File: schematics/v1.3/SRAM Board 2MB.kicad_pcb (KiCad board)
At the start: 2 copper layers, 125.7 x 33 mm, 48 parts, among them J1 Conn_01x01, J10 Conn_01x01, J11 Conn_01x01, J12 Conn_01x01, J13 Conn_01x01, J14 Conn_01x01, J15 Conn_01x01, J16 Conn_01x01, J17 Conn_01x01, J18 Conn_01x01, J19 Conn_01x01, J2 Conn_01x01, J20 Conn_01x01, J21 Conn_01x01, J22 Conn_01x01, J23 Conn_01x01, J24 Conn_01x01, J25 Conn_01x01, J26 Conn_01x01, J27 Conn_01x01, J28 Conn_01x01, J29 Conn_01x01, J3 Conn_01x01, J30 Conn_01x01, J31 Conn_01x01, J32 Conn_01x01, J4 Conn_01x01, J5 Conn_01x01, J6 Conn_01x01, J7 Conn_01x01, J8 Conn_01x01, J9 Conn_01x01, U1 74ABT00, U2 74ABT821ADW, U3 74ABT32, U34 74LS373, U4 CY62157ESL-45ZSXI, U5 CY62157ESL-45ZSXI, U6 74ABT373, U7 74AHCT1G79

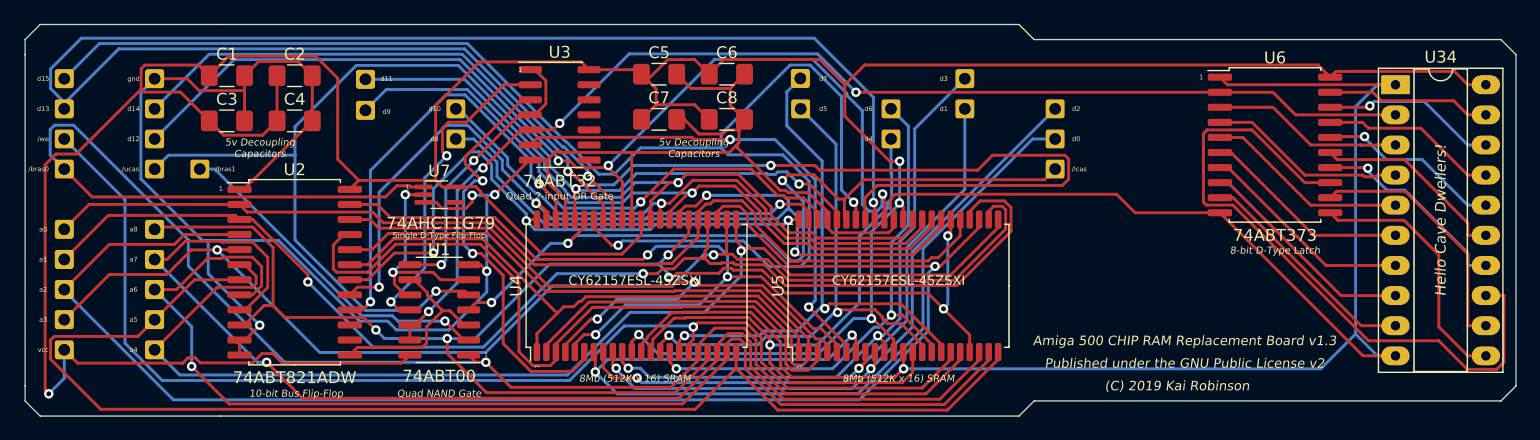
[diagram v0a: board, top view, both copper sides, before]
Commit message: Changed back to 2 layer board
Changed to 2 layer board, using thicker power traces and a copper fill on both sides for VCC and GND planes.
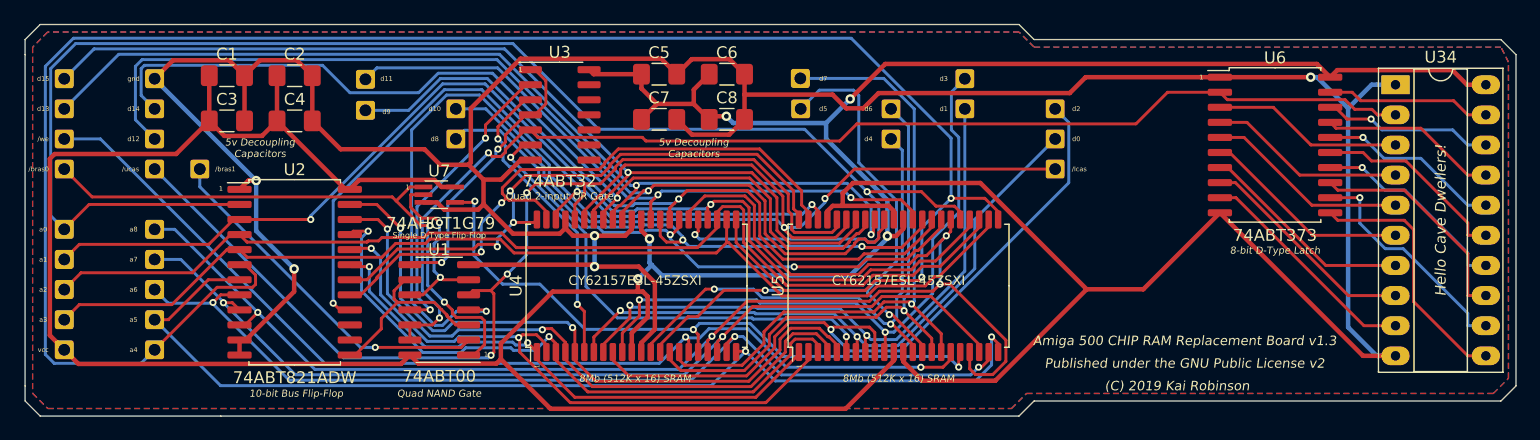
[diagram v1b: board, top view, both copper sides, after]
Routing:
- net /_bras0: track 132.7 -> 50.7 mm, vias 1 -> 2
- net /a4: track 96.9 -> 166.0 mm, vias 1 -> 2
- net /d13: track 142.0 -> 82.9 mm
- net /a18: track 0.00 -> 54.9 mm, vias 0 -> 3
- net /a0: track 86.9 -> 135.4 mm, vias 0 -> 2
- net /_lcas: track 68.5 -> 116.4 mm
- net /d15: track 123.7 -> 82.6 mm, vias 2 -> 1
- net /a2: track 129.1 -> 89.4 mm, vias 1 -> 0
- net /5d: track 57.0 -> 19.1 mm
- net /d14: track 112.5 -> 79.8 mm, vias 2 -> 1
- net /d0: track 78.7 -> 53.3 mm
- net /ma3: track 72.6 -> 52.5 mm, vias 0 -> 2
- net /a5: track 108.0 -> 88.9 mm, vias 0 -> 2
- net /a7: track 99.4 -> 81.7 mm, vias 1 -> 2
- net /a6: track 99.4 -> 81.8 mm, vias 1 -> 3
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- added copper zone on B.Cu, net GND
- added copper zone on F.Cu, net VCC
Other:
- net class Default: via_dia 0.8 -> 0.6; via_drill 0.4 -> 0.3
- net class Power added: clearance 0.2, trace_width 0.381, via_dia 0.8, via_drill 0.4
- rule trace_min: 0.2 -> 0.1
- rule via_min_drill: 0.3 -> 0.2

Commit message: New Board Layout
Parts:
- moved J18 64.5 mm to (218.9, 82.0)
- moved C8 47.8 mm to (245.4, 88.9), turned to 180 degrees
- moved C3 36.6 mm to (185.5, 100.6)
- moved C6 28.5 mm to (209.4, 100.6)
- moved C4 23.6 mm to (185.5, 83.2), turned to 180 degrees
- moved U1 23.1 mm to (160.4, 75.8)
- moved C7 17.0 mm to (209.4, 83.2), turned to 180 degrees
- moved U7 10.9 mm to (176.0, 73.4), turned to 180 degrees
- moved C1 10.8 mm to (156.5, 85.0), turned to 180 degrees
- moved U4 6.86 mm to (184.4, 91.9)
- moved U5 5.08 mm to (208.3, 91.9)
- moved C2 3.37 mm to (165.7, 73.4), turned to 90 degrees
- moved U3 2.43 mm to (186.5, 75.7)
- moved U2 1.89 mm to (162.0, 92.6), turned to 270 degrees
- moved C5 1.09 mm to (192.3, 73.4), turned to 270 degrees
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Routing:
- net VCC: track 289.3 -> 345.3 mm, vias 5 -> 6
- net /_bras1: track 30.0 -> 85.2 mm
- net GND: track 335.6 -> 280.9 mm, vias 5 -> 2
- net /a4: track 166.0 -> 121.6 mm, vias 2 -> 3
- net /clk: track 16.0 -> 60.0 mm
- net /a0: track 135.4 -> 92.0 mm, vias 2 -> 3
- net /a3: track 89.0 -> 127.7 mm, vias 0 -> 2
- net /d6: track 45.9 -> 80.0 mm
- net /_sramce: track 23.9 -> 53.3 mm, vias 2 -> 0
- net /a2: track 89.4 -> 114.7 mm, vias 0 -> 2
- net /a18: track 54.9 -> 76.5 mm, vias 3 -> 2
- net /d12: track 84.8 -> 66.5 mm
- net /d14: track 79.8 -> 66.1 mm
- net /d1: track 51.8 -> 64.7 mm
- net /_bras0: track 50.7 -> 38.4 mm, vias 2 -> 0
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- added copper zone on F.Cu, net GND
- removed copper zone on F.Cu, net VCC
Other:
- board text removed: "5v Decoupling Capacitors"
- board text removed: "Quad 2-input OR Gate"
- board text removed: "Quad NAND Gate"
